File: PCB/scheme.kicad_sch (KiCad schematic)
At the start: 12 parts, among them SW1 SW_Push, SW2 SW_Push, SW3 SW_Push, SW4 SW_Push, SW5 SW_Push, SW6 SW_Push, SW7 SW_Push, SW8 SW_Push, SW9 SW_Push, U1 XIAO-RP2040-DIP

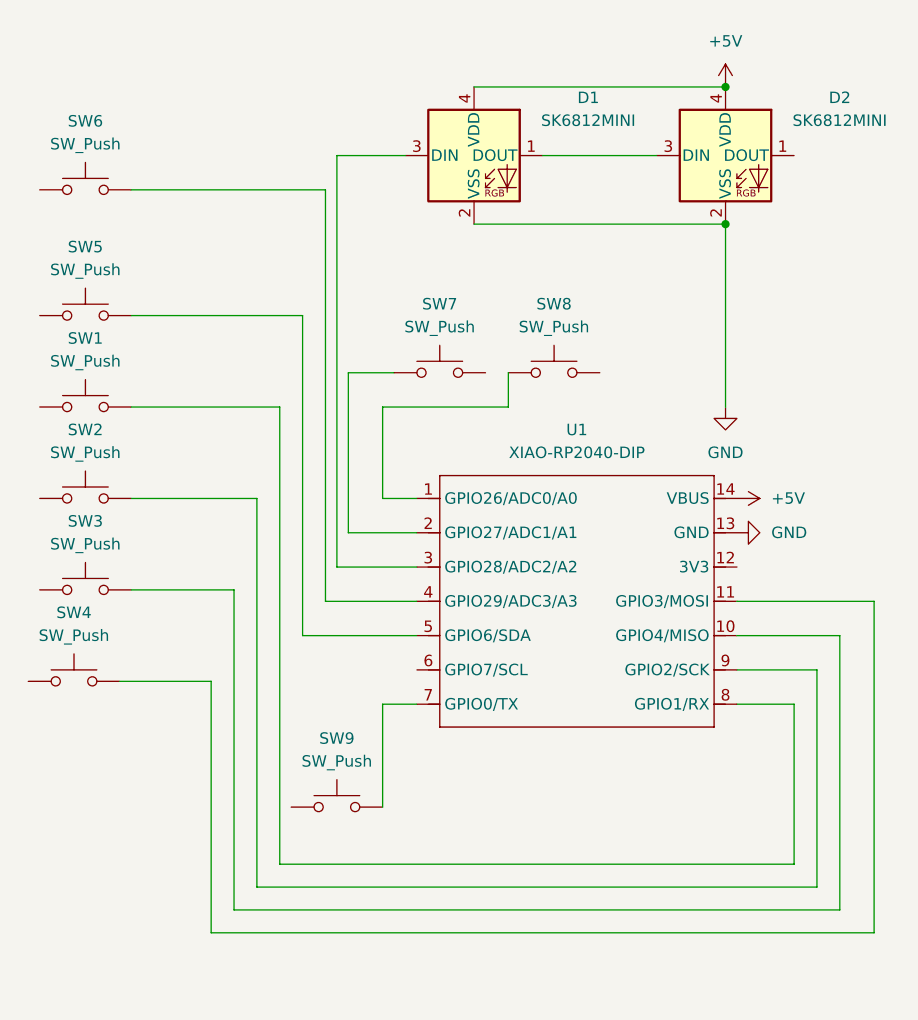
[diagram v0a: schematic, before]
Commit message: Update PCB schematic with junctions and power symbol
Added multiple junctions and wires to the schematic, modified switch positions, and replaced a switch with a power symbol for ground.
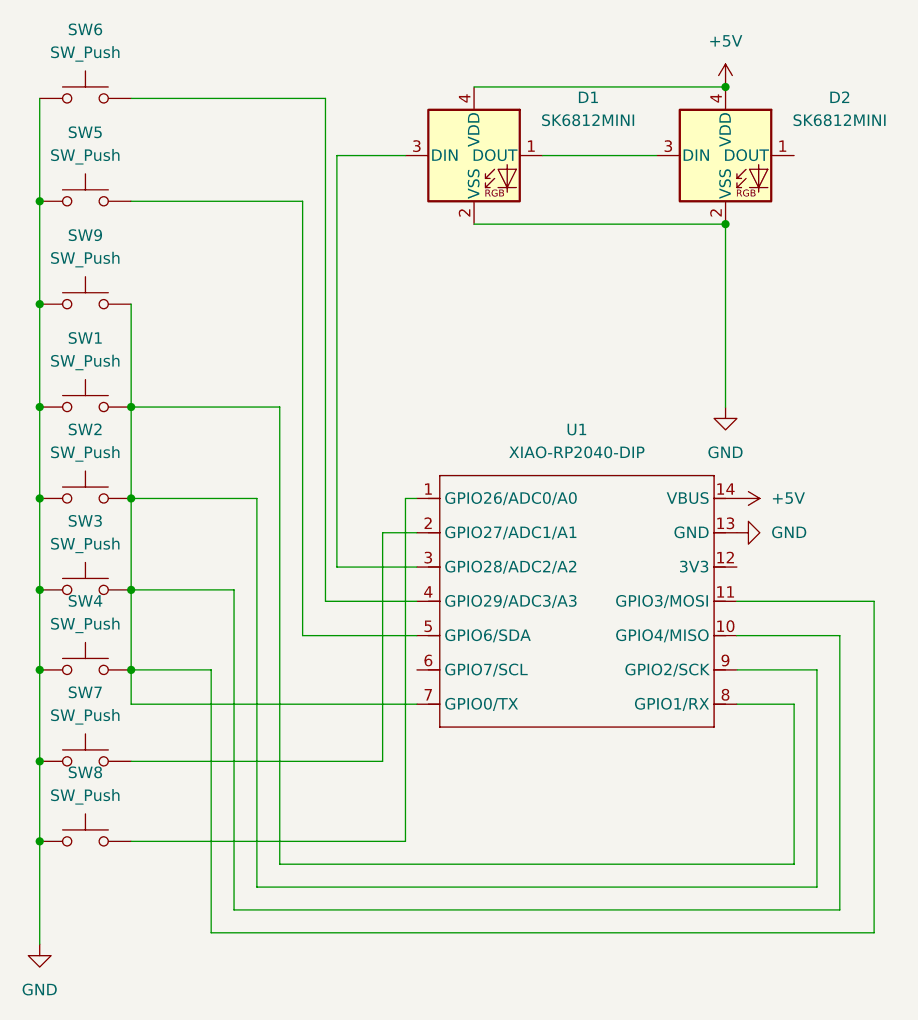
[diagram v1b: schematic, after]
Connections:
- net GND: now also SW1.2, SW2.1, SW3.1, SW4.1, SW5.2, SW6.2, SW7.1, SW8.2, SW9.2
- net at SW3.2, U1.10 (GPIO4/MISO): now also SW1.1, SW2.2, SW4.2, SW9.1, U1.11 (GPIO3/MOSI), U1.7 (GPIO0/TX), U1.8 (GPIO1/RX), U1.9 (GPIO2/SCK)
- net at U1.1 (GPIO26/ADC0/A0): now also SW8.1; no longer SW8.2
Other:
- moved on the sheet: SW4, SW5, SW6, SW8, SW9
